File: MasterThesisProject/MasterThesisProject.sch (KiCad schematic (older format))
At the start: 22 parts

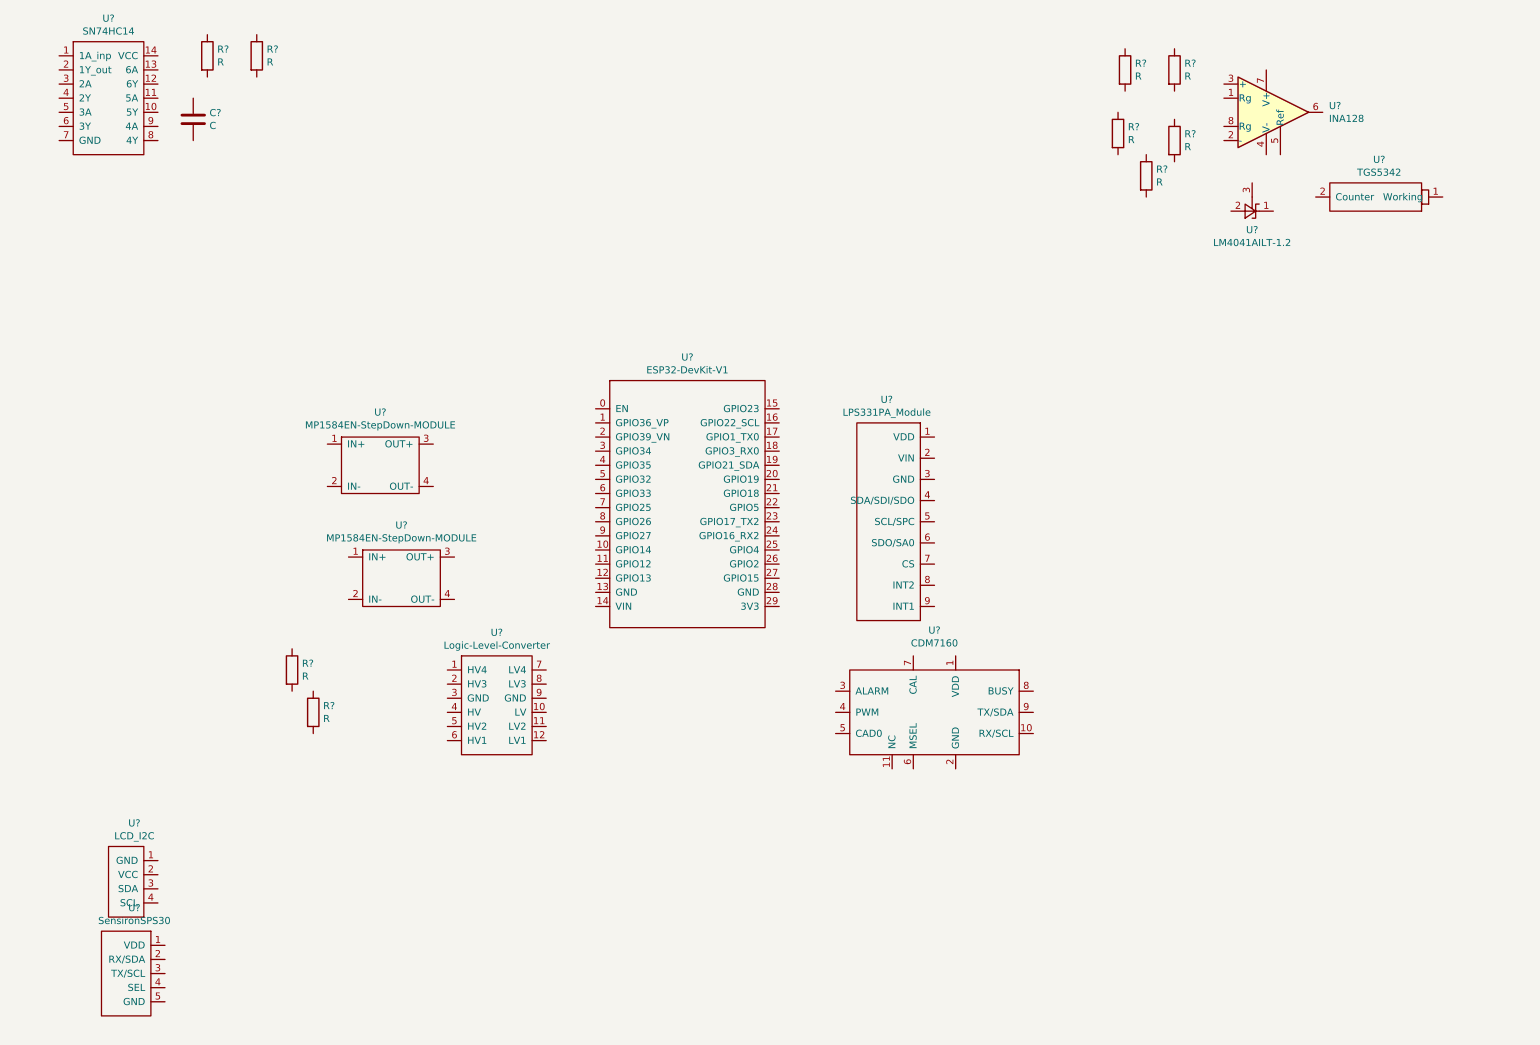
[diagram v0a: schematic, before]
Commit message: Add some electrical connections to the schematic
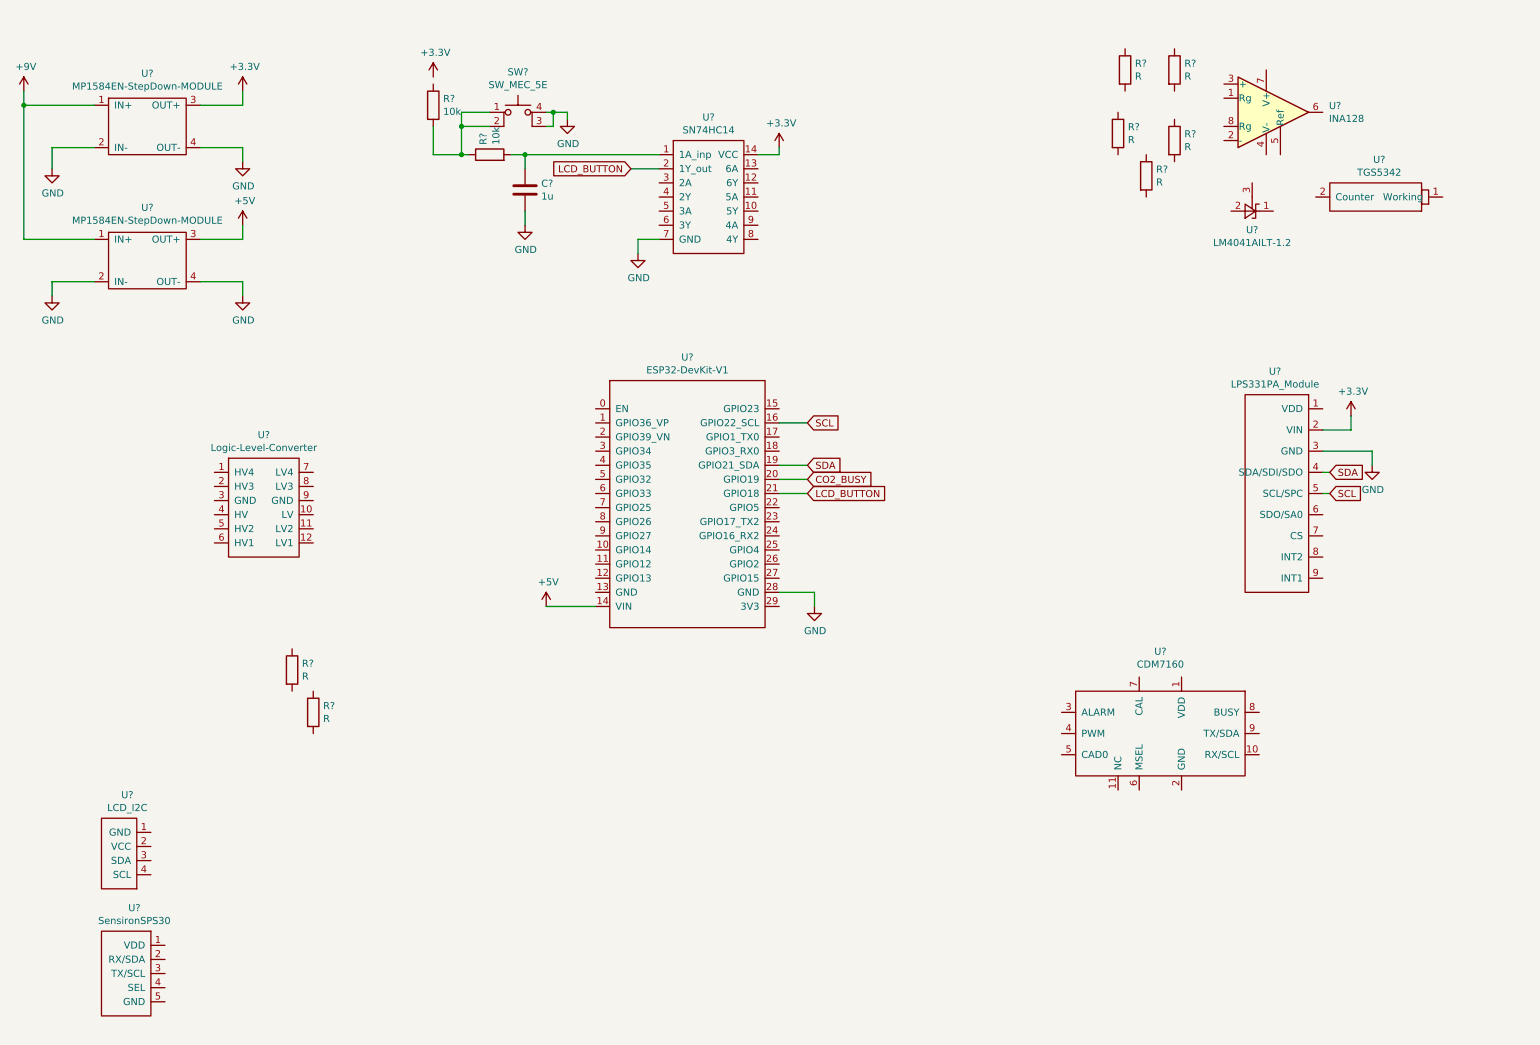
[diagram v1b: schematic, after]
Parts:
- added SW?: SW_MEC_5E, symbol Switch:SW_MEC_5E
- C?: value C -> 1u
- R? (x2): value R -> 10k
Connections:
- net +5V: now reaches U?.14 (VIN)
- net +5V: now also U?.3 (OUT+)
- net SCL: now reaches U?.16 (GPIO22_SCL)
- net SCL: now also U?.5 (SCL/SPC)
- net SDA: now reaches U?.19 (GPIO21_SDA)
- net SDA: now also U?.4 (SDA/SDI/SDO)
- net CO2_BUSY: now reaches U?.20 (GPIO19)
- net LCD_BUTTON: now reaches U?.21 (GPIO18)
- net LCD_BUTTON: now also U?.2 (1Y_out)
- net GND: now reaches U?.28 (GND)
- net GND: now also C?.2, U?.2 (IN-), U?.2 (IN-), U?.3 (GND), U?.4 (OUT-), U?.4 (OUT-), U?.7 (GND), SW?.3 (K), SW?.4 (A)
- net +3V3: now reaches U?.2 (VIN)
- net +3V3: now also U?.14 (VCC), U?.3 (OUT+)
- net +9V: now reaches U?.1 (IN+)
- net +9V: now also U?.1 (IN+)
- net at U?.1 (1A_inp): now also C?.1, R?.2
- net at R?.2: now also R?.1, SW?.1, SW?.2
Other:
- moved on the sheet: C?, R?, U?

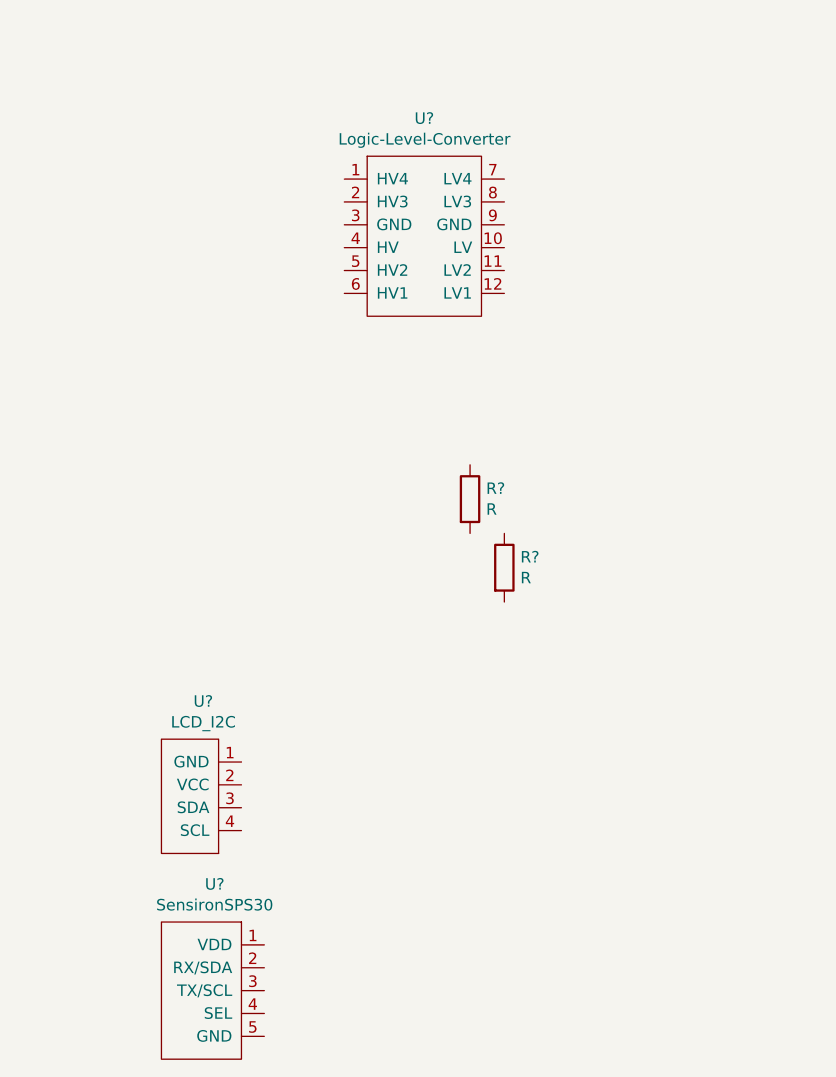
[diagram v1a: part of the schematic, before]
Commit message: Add more connections to schematic
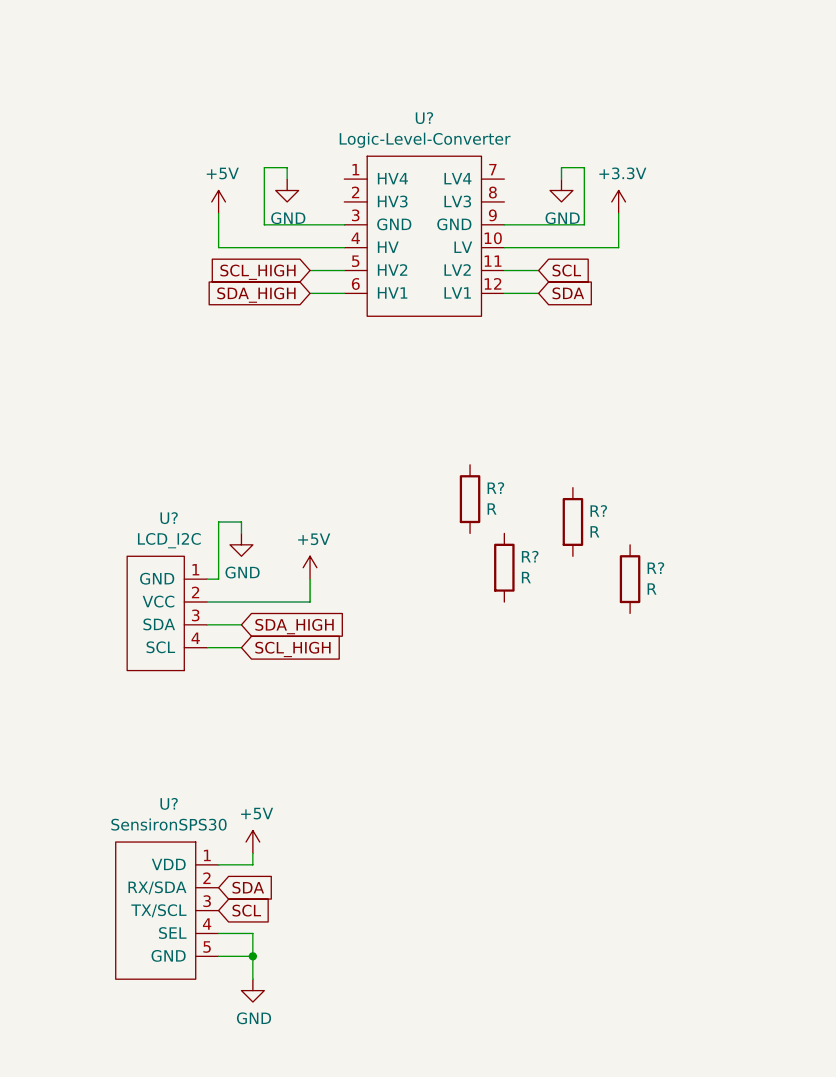
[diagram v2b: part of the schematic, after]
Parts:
- added R? (x2): R, symbol Device:R
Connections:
- net +3V3: now also U?.10 (LV)
- net +5V: now also U?.1 (VDD), U?.2 (VCC), U?.4 (HV)
- net GND: now also U?.1 (GND), U?.3 (GND), U?.4 (SEL), U?.5 (GND), U?.9 (GND)
- net SCL: now also U?.11 (LV2), U?.3 (TX/SCL)
- net SDA: now also U?.12 (LV1), U?.2 (RX/SDA)
- net SCL_HIGH: now reaches U?.5 (HV2)
- net SCL_HIGH: now also U?.4 (SCL)
- net SDA_HIGH: now reaches U?.6 (HV1)
- net SDA_HIGH: now also U?.3 (SDA)
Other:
- moved on the sheet: U?
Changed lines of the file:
@@
 L AirControl:SensironSPS30 U?
 U 1 1 60524666
-P 1400 7650
-F 0 "U?" H 1433 8465 50  0000 C CNN
-F 1 "SensironSPS30" H 1433 8374 50  0000 C CNN
-F 2 "" H 1400 7650 50  0001 C CNN
-F 3 "" H 1400 7650 50  0001 C CNN
-	1    1400 7650
+P 1200 7300
+F 0 "U?" H 1233 8115 50  0000 C CNN
+F 1 "SensironSPS30" H 1233 8024 50  0000 C CNN
+F 2 "" H 1200 7300 50  0001 C CNN
+F 3 "" H 1200 7300 50  0001 C CNN
+	1    1200 7300
 	1    0    0    -1
 $EndComp
@@
 L AirControl:LCD_I2C U?
 U 1 1 60526915
-P 1350 6750
-F 0 "U?" H 1383 7465 50  0000 C CNN
-F 1 "LCD_I2C" H 1383 7374 50  0000 C CNN
-F 2 "" H 1350 6750 50  0001 C CNN
-F 3 "" H 1350 6750 50  0001 C CNN
-	1    1350 6750
+P 1200 5950
+F 0 "U?" H 1233 6665 50  0000 C CNN
+F 1 "LCD_I2C" H 1233 6574 50  0000 C CNN
+F 2 "" H 1200 5950 50  0001 C CNN
+F 3 "" H 1200 5950 50  0001 C CNN
+	1    1200 5950
 	1    0    0    -1
 $EndComp
@@
 Wire Wire Line
 	9850 3900 9900 3900
+Wire Wire Line
+	2700 4250 2850 4250
+Wire Wire Line
+	2700 4150 2850 4150
+Text GLabel 2850 4250 2    50   Input ~ 0
+SDA
+Text GLabel 2850 4150 2    50   Input ~ 0
+SCL
+Wire Wire Line
+	2000 4150 1850 4150
+Wire Wire Line
+	2000 4250 1850 4250
+Text GLabel 1850 4150 0    50   Input ~ 0
+SCL_HIGH
+Text GLabel 1850 4250 0    50   Input ~ 0
+SDA_HIGH
+$Comp
+L power:+3.3V #PWR?
+U 1 1 60576F46
+P 3200 3900
+F 0 "#PWR?" H 3200 3750 50  0001 C CNN
+F 1 "+3.3V" H 3215 4073 50  0000 C CNN
+F 2 "" H 3200 3900 50  0001 C CNN
+F 3 "" H 3200 3900 50  0001 C CNN
+	1    3200 3900
+	1    0    0    -1
+$EndComp
+$Comp
+L power:+5V #PWR?
+U 1 1 605785E3
+P 1450 3900
+F 0 "#PWR?" H 1450 3750 50  0001 C CNN
+F 1 "+5V" H 1465 4073 50  0000 C CNN
+F 2 "" H 1450 3900 50  0001 C CNN
+F 3 "" H 1450 3900 50  0001 C CNN
+	1    1450 3900
+	1    0    0    -1
+$EndComp
+$Comp
+L power:GND #PWR?
+U 1 1 6057939A
+P 1750 3750
+F 0 "#PWR?" H 1750 3500 50  0001 C CNN
+F 1 "GND" H 1755 3577 50  0000 C CNN
+F 2 "" H 1750 3750 50  0001 C CNN
+F 3 "" H 1750 3750 50  0001 C CNN
+	1    1750 3750
+	1    0    0    -1
+$EndComp
+$Comp
+L power:GND #PWR?
+U 1 1 6057A370
+P 2950 3750
+F 0 "#PWR?" H 2950 3500 50  0001 C CNN
+F 1 "GND" H 2955 3577 50  0000 C CNN
+F 2 "" H 2950 3750 50  0001 C CNN
+F 3 "" H 2950 3750 50  0001 C CNN
+	1    2950 3750
+	1    0    0    -1
+$EndComp
+Wire Wire Line
+	2000 4050 1450 4050
+Wire Wire Line
+	1450 4050 1450 3900
+Wire Wire Line
+	2700 4050 3200 4050
+Wire Wire Line
+	3200 4050 3200 3900
+Wire Wire Line
+	2950 3750 2950 3700
+Wire Wire Line
+	2950 3700 3050 3700
+Wire Wire Line
+	3050 3700 3050 3950
+Wire Wire Line
+	3050 3950 2700 3950
+Wire Wire Line
+	2000 3950 1650 3950
+Wire Wire Line
+	1650 3950 1650 3700
+Wire Wire Line
+	1650 3700 1750 3700
+Wire Wire Line
+	1750 3700 1750 3750
+$Comp
+L power:GND #PWR?
+U 1 1 60589710
+P 1550 5300
+F 0 "#PWR?" H 1550 5050 50  0001 C CNN
+F 1 "GND" H 1555 5127 50  0000 C CNN
+F 2 "" H 1550 5300 50  0001 C CNN
+F 3 "" H 1550 5300 50  0001 C CNN
+	1    1550 5300
+	1    0    0    -1
+$EndComp
+$Comp
+L power:GND #PWR?
+U 1 1 6058AAA2
+P 1600 7250
+F 0 "#PWR?" H 1600 7000 50  0001 C CNN
+F 1 "GND" H 1605 7077 50  0000 C CNN
+F 2 "" H 1600 7250 50  0001 C CNN
+F 3 "" H 1600 7250 50  0001 C CNN
+	1    1600 7250
+	1    0    0    -1
+$EndComp
+$Comp
+L power:+5V #PWR?
+U 1 1 6058B4F6
+P 1850 5500
+F 0 "#PWR?" H 1850 5350 50  0001 C CNN
+F 1 "+5V" H 1865 5673 50  0000 C CNN
+F 2 "" H 1850 5500 50  0001 C CNN
+F 3 "" H 1850 5500 50  0001 C CNN
+	1    1850 5500
+	1    0    0    -1
+$EndComp
+$Comp
+L power:+5V #PWR?
+U 1 1 6058C191
+P 1600 6700
+F 0 "#PWR?" H 1600 6550 50  0001 C CNN
+F 1 "+5V" H 1615 6873 50  0000 C CNN
+F 2 "" H 1600 6700 50  0001 C CNN
+F 3 "" H 1600 6700 50  0001 C CNN
+	1    1600 6700
+	1    0    0    -1
+$EndComp
+Wire Wire Line
+	1450 7150 1600 7150
+Wire Wire Line
+	1600 7150 1600 7250
+Wire Wire Line
+	1450 6750 1600 6750
+Wire Wire Line
+	1600 6750 1600 6700
+Wire Wire Line
+	1400 5500 1450 5500
+Wire Wire Line
+	1450 5500 1450 5250
+Wire Wire Line
+	1450 5250 1550 5250
+Wire Wire Line
+	1550 5250 1550 5300
+Wire Wire Line
+	1850 5500 1850 5600
+Wire Wire Line
+	1850 5600 1400 5600
+Wire Wire Line
+	1400 5800 1550 5800
+Wire Wire Line
+	1400 5700 1550 5700
+Text GLabel 1550 5800 2    50   Input ~ 0
+SCL_HIGH
+Text GLabel 1550 5700 2    50   Input ~ 0
+SDA_HIGH
+Text GLabel 1450 6850 2    50   Input ~ 0
+SDA
+Text GLabel 1450 6950 2    50   Input ~ 0
+SCL
+Wire Wire Line
+	1450 7050 1600 7050
+Wire Wire Line
+	1600 7050 1600 7150
+Connection ~ 1600 7150
+$Comp
+L Device:R R?
+U 1 1 605997BB
+P 3000 5250
+F 0 "R?" H 3070 5296 50  0000 L CNN
+F 1 "R" H 3070 5205 50  0000 L CNN
+F 2 "" V 2930 5250 50  0001 C CNN
+F 3 "~" H 3000 5250 50  0001 C CNN
+	1    3000 5250
+	1    0    0    -1
+$EndComp
+$Comp
+L Device:R R?
+U 1 1 6059A344
+P 3250 5500
+F 0 "R?" H 3320 5546 50  0000 L CNN
+F 1 "R" H 3320 5455 50  0000 L CNN
+F 2 "" V 3180 5500 50  0001 C CNN
+F 3 "~" H 3250 5500 50  0001 C CNN
+	1    3250 5500
+	1    0    0    -1
+$EndComp
 $EndSCHEMATC

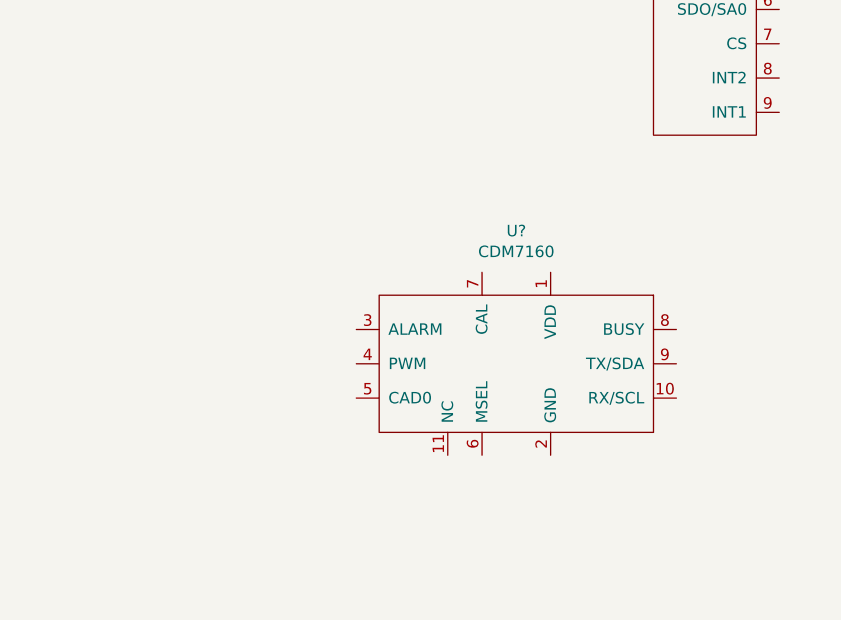
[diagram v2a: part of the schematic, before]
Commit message: Update CDM7160, put new at the schematic
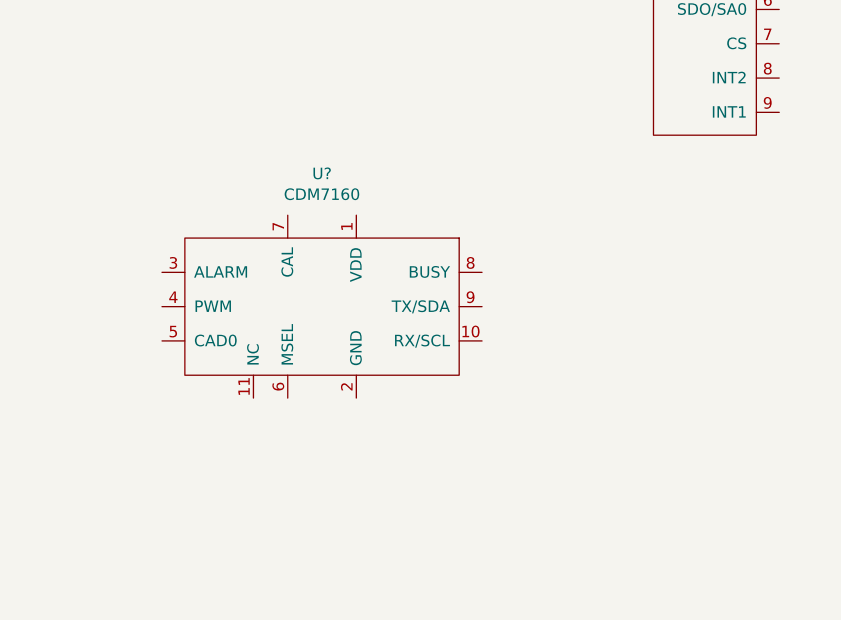
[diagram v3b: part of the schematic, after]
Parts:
- removed U?: CDM7160, symbol AirControl:CDM7160
- added U?: CDM7160, symbol AirControl:CDM7160
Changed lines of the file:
@@
-$EndComp
-$Comp
-L AirControl:CDM7160 U?
-U 1 1 605201CF
-P 8700 5600
-F 0 "U?" H 8700 6181 50  0000 C CNN
-F 1 "CDM7160" H 8700 6090 50  0000 C CNN
-F 2 "" H 9050 5150 50  0001 C CNN
-F 3 "" H 9050 5150 50  0001 C CNN
-	1    8700 5600
-	1    0    0    -1
 $EndComp
 $Comp
@@
 	1    0    0    -1
 $EndComp
+$Comp
+L AirControl:CDM7160 U?
+U 1 1 605A029F
+P 7850 5350
+F 0 "U?" H 7850 5931 50  0000 C CNN
+F 1 "CDM7160" H 7850 5840 50  0000 C CNN
+F 2 "" H 8200 4900 50  0001 C CNN
+F 3 "" H 8200 4900 50  0001 C CNN
+	1    7850 5350
+	1    0    0    -1
+$EndComp
